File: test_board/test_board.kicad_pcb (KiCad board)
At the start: 4 copper layers, 62 x 54.4 mm, 57 parts, among them J1 Screw_Terminal_01x02, J2 USB_B_Micro, J3 I2C1, J4 USART2, J5 SWD, J6 USART6, J7 CAN1, J8 USART3, Q1 AO3401A, SW1 SW_SPDT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

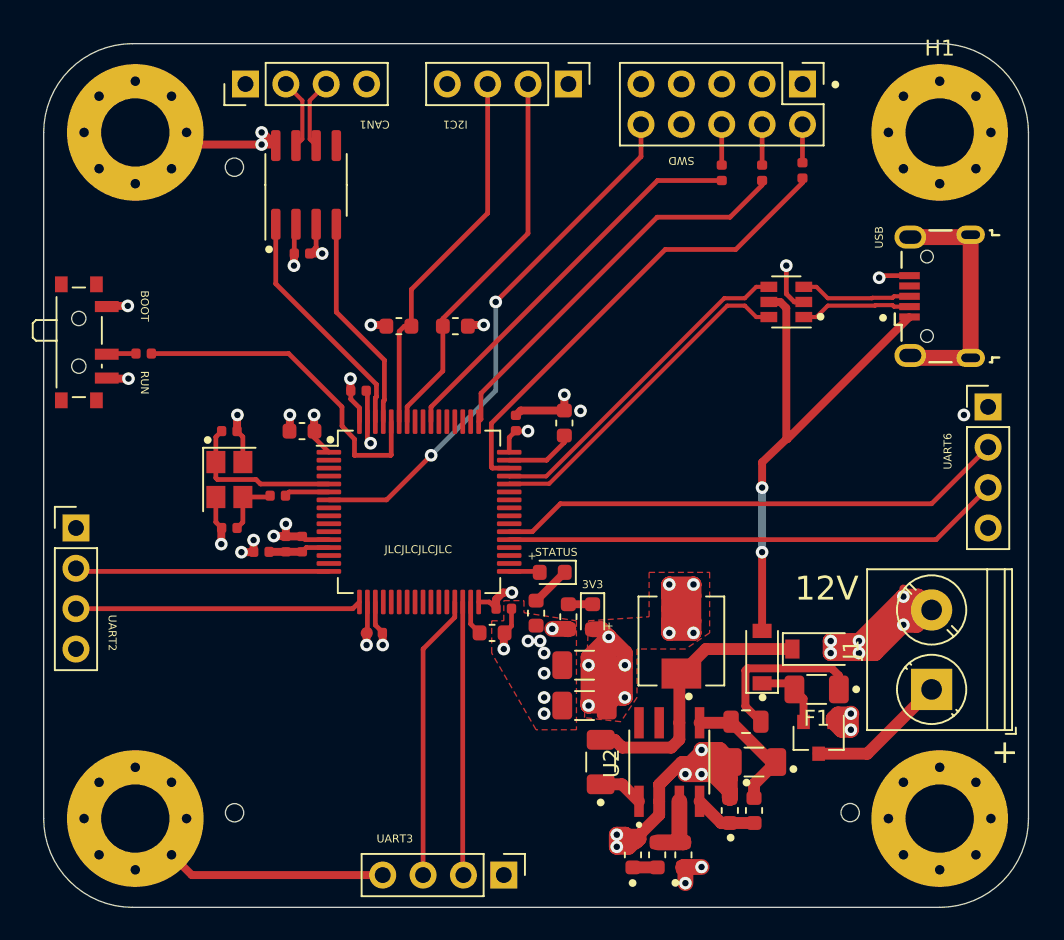
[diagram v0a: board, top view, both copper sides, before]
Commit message: Replace MD3579DJ with LM2576-ADJ
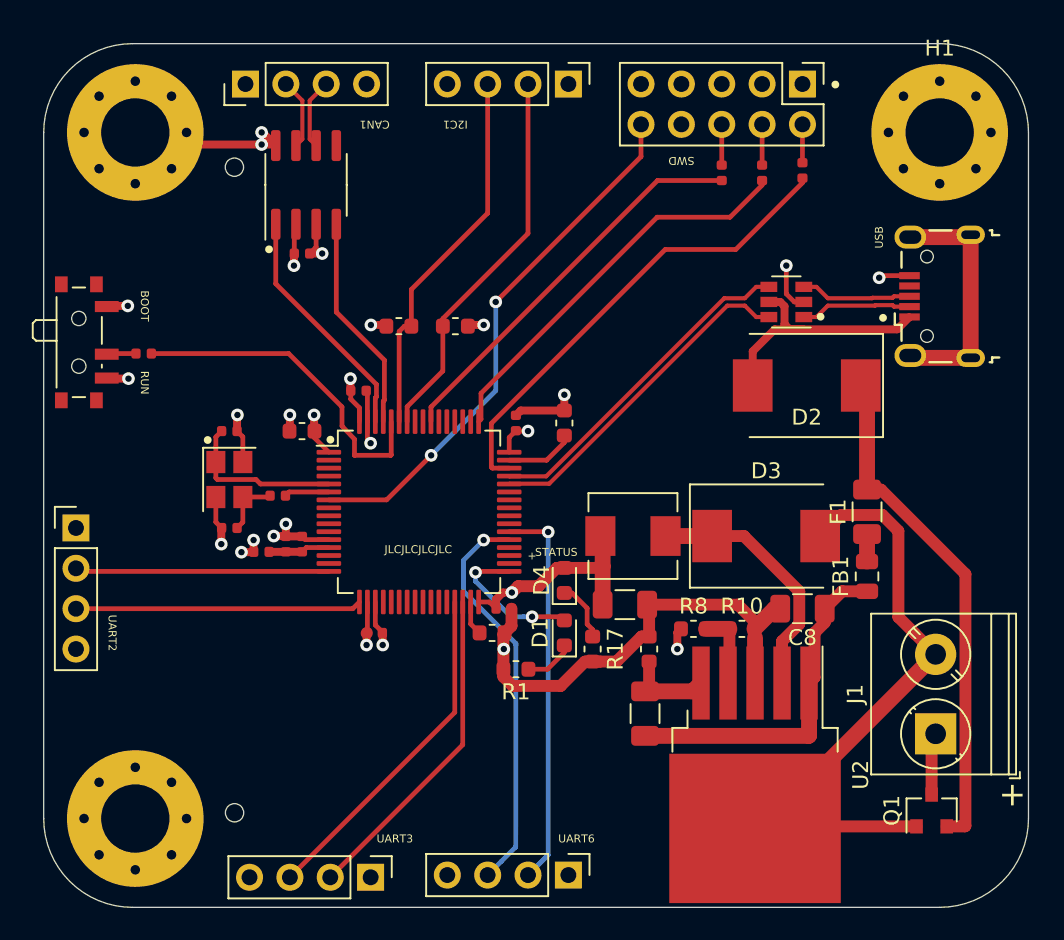
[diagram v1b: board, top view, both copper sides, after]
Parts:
- removed C14: 10n, Capacitor_SMD:C_1206_3216Metric
- removed C16: 10u, Capacitor_SMD:C_1206_3216Metric
- removed H2: MountingHole_Pad, MountingHole:MountingHole_4.3mm_M4_Pad_Via
- removed R2: 100k, Resistor_SMD:R_0603_1608Metric
- removed R9: 15k, Resistor_SMD:R_0603_1608Metric
- added C6: 100n, Capacitor_SMD:C_1206_3216Metric, F.Cu at (63.8, 124.5)
- C15: value 10u -> 1000u
- C8, L2: value 10u -> 100u
- D2, D3: value B5819W -> SS34; footprint Diode_SMD:D_SOD-123 -> Diode_SMD:D_SMC
- R10: value 270 -> 1k
- R3: value 68k -> 47k
- R8: value 47k -> 1k7
- U2: value MP2359DJ-LF-Z -> LM2576S-ADJ; footprint MyKiCADFootprints:SOIC127P599X175-8N -> Package_TO_SOT_SMD:TO-263-5_TabPin3
- moved J6 39.6 mm to (58.9, 134.6), turned to 270 degrees
- moved D2 17.3 mm to (73.9, 103.8), turned to 180 degrees
- moved R10 15.8 mm to (69.8, 119.1), turned to 0 degrees
- moved R8 14.2 mm to (66.8, 119.1), turned to 0 degrees
- moved FB1 11.9 mm to (77.7, 115.8), turned to 90 degrees
- moved F1 11.6 mm to (77.7, 111.8), turned to 90 degrees
- moved R3 11.4 mm to (64.0, 120.4)
- moved C8 10.1 mm to (73.7, 117.9)
- moved Q1 8.45 mm to (81.8, 130.6), turned to 90 degrees
- moved J8 8.38 mm to (46.5, 134.8)
- moved D3 7.84 mm to (71.4, 113.3)
- moved L2 7.27 mm to (63.0, 113.3), turned to 180 degrees
- moved U2 5.46 mm to (70.7, 128.3), turned to 270 degrees
- moved C15 4.58 mm to (62.5, 117.6), turned to 0 degrees
- moved D1 3.89 mm to (58.7, 119.4), turned to 90 degrees
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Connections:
- net +12V renamed +24V
- R10 pad 1: Net-(R10-Pad1) -> BUCK_FB
- U2 pad 1: BUCK_BST -> BUCK_IN
- U2 pad 2: GND -> BUCK_SW
- U2 pad 3: BUCK_FB -> GND
- U2 pad 4: BUCK_EN -> BUCK_FB
- U2 pad 5: BUCK_IN -> BUCK_EN
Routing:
- net +3V3: track 92.8 -> 57.7 mm, vias 23 -> 12
- net Net-(D2-Pad1): track 4.48 -> 32.1 mm
- net +5V: track 33.2 -> 16.5 mm, vias 2 -> 0
- net BUCK_IN: track 8.75 -> 21.8 mm
- net GND: track 128.6 -> 119.0 mm, vias 36 -> 15
- net Net-(F1-Pad1): track 10.6 -> 1.73 mm
- net LED_STATUS: track 1.94 -> 9.32 mm, vias 0 -> 2
- net USART6_RX: track 32.3 -> 26.2 mm, vias 0 -> 1
- net USART6_TX: track 31.5 -> 25.4 mm, vias 0 -> 1
- net +24V: track 8.79 -> 3.93 mm
- net USART3_RX: track 18.0 -> 21.6 mm
- net USART3_TX: track 17.3 -> 20.8 mm
- net BUCK_BST: track 2.86 -> 0.00 mm
- net Net-(D4-Pad1): track 1.52 -> 3.76 mm
- net BUCK_EN: track 3.99 -> 5.72 mm
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- removed copper zone on F.Cu, net +3V3
- removed copper zone on F.Cu, net GND
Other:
- outline, holes or cut-outs redrawn
- board text removed: "12V"
- board text removed: "3V3"
